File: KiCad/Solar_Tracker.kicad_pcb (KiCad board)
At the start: 2 copper layers, 160 x 100 mm, 116 parts, among them J1 +48V, J10 AZJMP, J11 ELJMP, J12 AZ, J13 CONN_01X03, J2 HOLE, J3 HOLE, J4 EL, J5 HOLE, J6 HOLE, J7 CONN_01X05, J8 GPIO, J9 GPIO, Q1 BUK9M42-60E, Q2 BUK9M42-60E, Q3 BUK9M42-60E, Q4 BUK9M42-60E, Q5 BUK9M42-60E, Q6 BUK9M42-60E, Q7 BUK9M42-60E, Q8 BUK9M42-60E, U1 MER1S4805SC, U10 TLP291, U11 75LBC182, U12 A4927, U2 A4927, U3 Nano, U4 A4927, U5 A4927, U6 MER1S4805SC, U7 TLP291, U8 TLP291, U9 TLP291

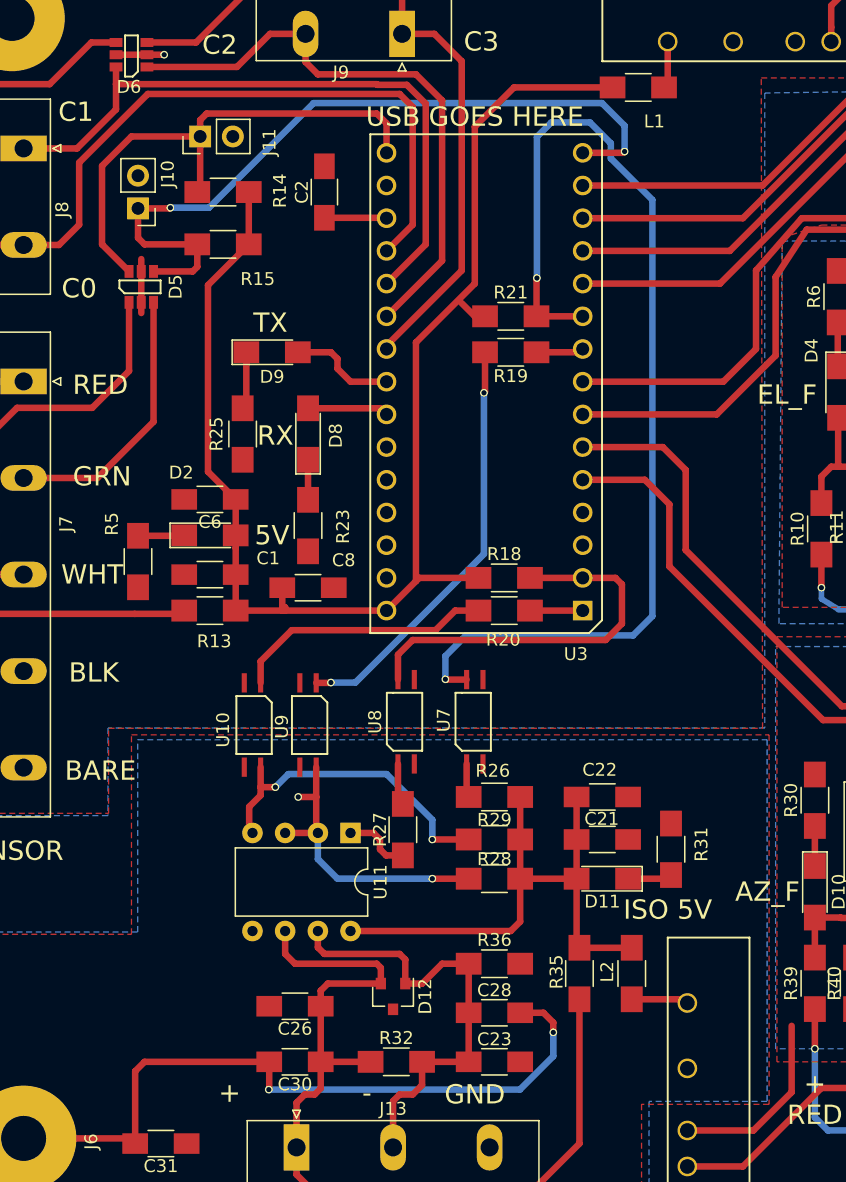
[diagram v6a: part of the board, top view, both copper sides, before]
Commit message: updated RS-485
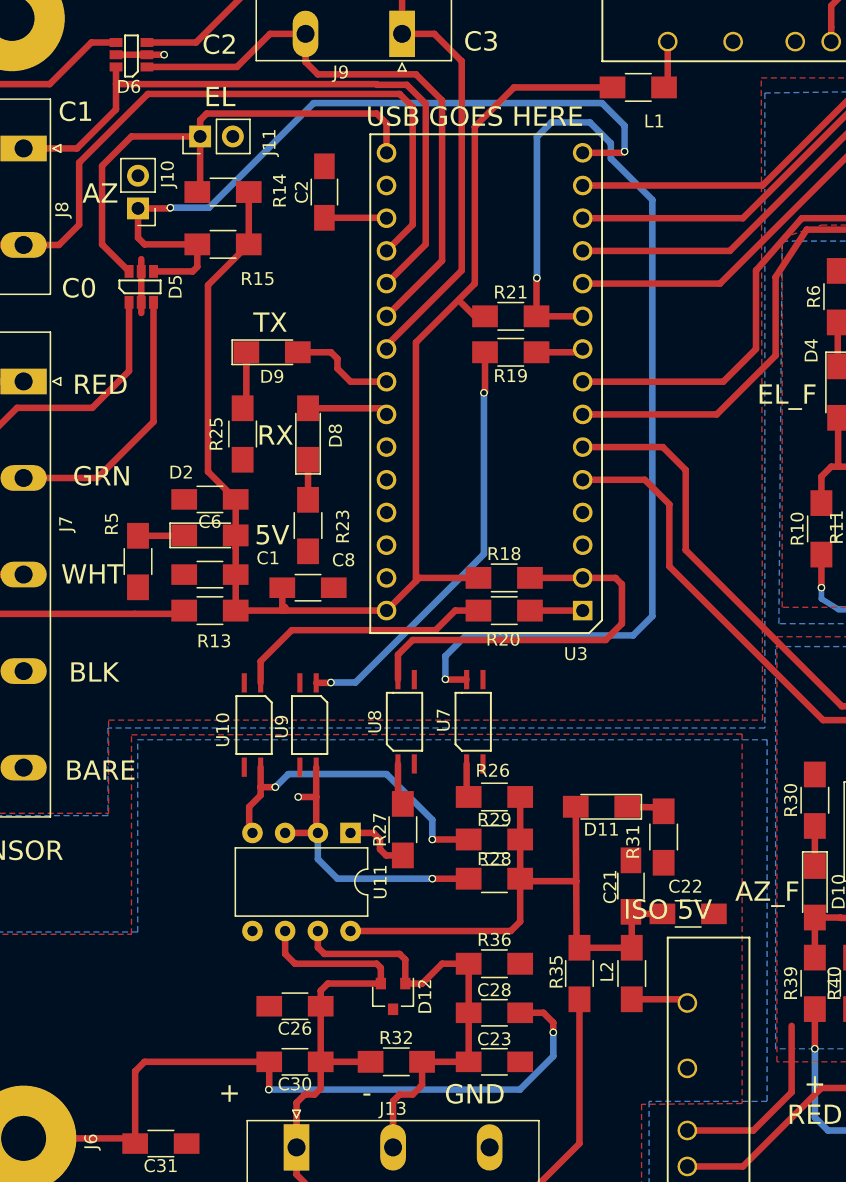
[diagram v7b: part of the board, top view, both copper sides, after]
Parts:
- moved C22 11.3 mm to (70.4, 87.1)
- moved D11 5.59 mm to (63.7, 78.7)
- moved C21 4.25 mm to (66.0, 84.9), turned to 90 degrees
- moved R31 1.11 mm to (68.5, 81.1), turned to 270 degrees
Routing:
- net GND: track 257.3 -> 159.7 mm
- net (no net): track 59.5 -> 157.1 mm
- net +5VD: track 44.2 -> 48.4 mm
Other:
- board text added: "AZ"
- board text added: "CWRU EECS"
- board text added: "EL"
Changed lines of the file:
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@@
   (general
     (links 321)
-    (no_connects 14)
+    (no_connects 15)
     (area 11.924999 11.924999 172.075001 112.075001)
     (thickness 1.6)
-    (drawings 39)
-    (tracks 901)
+    (drawings 42)
+    (tracks 904)
     (zones 0)
     (modules 116)
@@
   )
   (module Capacitors_SMD:C_1206_HandSoldering (layer F.Cu)
-    (at 63.754 81.28)
+    (at 65.9765 84.8995 90)
     (descr "Capacitor SMD 1206, hand soldering")
     (tags "capacitor 1206")
     (attr smd)
-    (fp_text reference C21 (at -0.0508 -1.6002) (layer F.SilkS)
+    (fp_text reference C21 (at -0.0508 -1.6002 90) (layer F.SilkS)
       (effects (font (size 1 1) (thickness 0.15)))
     )
-    (fp_text value 10u (at 0 2) (layer F.Fab)
+    (fp_text value 10u (at 0 2 90) (layer F.Fab)
       (effects (font (size 1 1) (thickness 0.15)))
     )
-    (fp_text user %R (at 0 -1.75) (layer F.Fab)
+    (fp_text user %R (at 0 -1.75 90) (layer F.Fab)
       (effects (font (size 1 1) (thickness 0.15)))
     )
@@
     (fp_line (start 3.25 1.05) (end 3.25 -1.05) (layer F.CrtYd) (width 0.05))
     (fp_line (start 3.25 1.05) (end -3.25 1.05) (layer F.CrtYd) (width 0.05))
-    (pad 1 smd rect (at -2 0) (size 2 1.6) (layers F.Cu F.Paste F.Mask)
+    (pad 1 smd rect (at -2 0 90) (size 2 1.6) (layers F.Cu F.Paste F.Mask)
       (net 14 +5VD))
-    (pad 2 smd rect (at 2 0) (size 2 1.6) (layers F.Cu F.Paste F.Mask)
+    (pad 2 smd rect (at 2 0 90) (size 2 1.6) (layers F.Cu F.Paste F.Mask)
       (net 15 GNDD))
     (model Capacitors_SMD.3dshapes/C_1206.wrl
@@
   )
   (module Capacitors_SMD:C_1206_HandSoldering (layer F.Cu)
-    (at 63.754 77.978)
+    (at 70.4215 87.0585)
     (descr "Capacitor SMD 1206, hand soldering")
     (tags "capacitor 1206")
@@
   )
   (module LEDs:LED_1206_HandSoldering (layer F.Cu)
-    (at 63.754 84.328 180)
+    (at 63.6905 78.74 180)
     (descr "LED SMD 1206, hand soldering")
     (tags "LED 1206")
@@
   )
   (module Resistors_SMD:R_1206_HandSoldering (layer F.Cu)
-    (at 69.088 82.042 90)
+    (at 68.5165 81.0895 270)
     (descr "Resistor SMD 1206, hand soldering")
     (tags "resistor 1206")
     (attr smd)
-    (fp_text reference R31 (at 0.381 2.3622 90) (layer F.SilkS)
+    (fp_text reference R31 (at 0.381 2.3622 270) (layer F.SilkS)
       (effects (font (size 1 1) (thickness 0.15)))
     )
-    (fp_text value 150 (at 0 1.9 90) (layer F.Fab)
+    (fp_text value 150 (at 0 1.9 270) (layer F.Fab)
       (effects (font (size 1 1) (thickness 0.15)))
     )
-    (fp_text user %R (at 0 0 90) (layer F.Fab)
+    (fp_text user %R (at 0 0 270) (layer F.Fab)
       (effects (font (size 0.7 0.7) (thickness 0.105)))
     )
@@
     (fp_line (start 3.25 1.1) (end 3.25 -1.11) (layer F.CrtYd) (width 0.05))
     (fp_line (start 3.25 1.1) (end -3.25 1.1) (layer F.CrtYd) (width 0.05))
-    (pad 1 smd rect (at -2 0 90) (size 2 1.7) (layers F.Cu F.Paste F.Mask)
+    (pad 1 smd rect (at -2 0 270) (size 2 1.7) (layers F.Cu F.Paste F.Mask)
       (net 27 "Net-(D11-Pad1)"))
-    (pad 2 smd rect (at 2 0 90) (size 2 1.7) (layers F.Cu F.Paste F.Mask)
+    (pad 2 smd rect (at 2 0 270) (size 2 1.7) (layers F.Cu F.Paste F.Mask)
       (net 15 GNDD))
     (model ${KISYS3DMOD}/Resistors_SMD.3dshapes/R_1206.wrl
@@
     )
   )
+  (gr_text EL (at 34.036 23.622) (layer F.SilkS)
+    (effects (font (size 1.5 1.5) (thickness 0.3)))
+  )
+  (gr_text AZ (at 24.765 31.115) (layer F.SilkS)
+    (effects (font (size 1.5 1.5) (thickness 0.3)))
+  )
+  (gr_text "CWRU EECS" (at 83.312 60.833) (layer B.SilkS)
+    (effects (font (size 12.7 12.7) (thickness 0.3)) (justify mirror))
+  )
   (gr_text "Documentation Available At:\nhttps://github.com/wnourse05/Lake_Metroparks_Farmpark_Solar_Tracker" (at 159.766 108.077) (layer F.SilkS)
     (effects (font (size 1.5 1.1) (thickness 0.275)) (justify right))
@@
   (segment (start 97.282 61.722) (end 97.282 66.802) (width 3.81) (layer F.Cu) (net 0))
   (segment (start 97.282 66.802) (end 97.663 67.183) (width 3.81) (layer F.Cu) (net 0))
+  (segment (start 169.799 66.929) (end 169.799 29.083) (width 0.508) (layer F.Cu) (net 0))
+  (segment (start 115.697 16.383) (end 115.443 16.129) (width 0.508) (layer F.Cu) (net 0))
+  (segment (start 157.099 16.383) (end 115.697 16.383) (width 0.508) (layer F.Cu) (net 0))
+  (segment (start 169.799 29.083) (end 157.099 16.383) (width 0.508) (layer F.Cu) (net 0))
   (segment (start 37.846 100.711) (end 57.3532 100.711) (width 0.508) (layer B.Cu) (net 1))
   (segment (start 37.878 98.552) (end 37.878 100.679) (width 0.508) (layer F.Cu) (net 1))
@@
   (segment (start 89.916 88.362532) (end 89.916 90.456) (width 0.508) (layer F.Cu) (net 13))
   (segment (start 88.99 87.436532) (end 89.916 88.362532) (width 0.508) (layer F.Cu) (net 13))
+  (segment (start 68.4215 87.0585) (end 66.1355 87.0585) (width 0.508) (layer F.Cu) (net 14) (status C00000))
+  (segment (start 66.1355 87.0585) (end 66.04 87.154) (width 0.508) (layer F.Cu) (net 14) (status C00000))
+  (segment (start 66.04 87.154) (end 66.04 89.694) (width 0.508) (layer F.Cu) (net 14) (status C00000))
+  (segment (start 61.724693 84.518886) (end 57.562886 84.518886) (width 0.508) (layer F.Cu) (net 14))
+  (segment (start 57.562886 84.518886) (end 57.372 84.328) (width 0.508) (layer F.Cu) (net 14))
   (segment (start 44.196 88.392) (end 56.642 88.392) (width 0.508) (layer F.Cu) (net 14))
   (segment (start 57.372 87.662) (end 57.372 84.328) (width 0.508) (layer F.Cu) (net 14))
   (segment (start 56.642 88.392) (end 57.372 87.662) (width 0.508) (layer F.Cu) (net 14))
   (segment (start 61.436 89.154) (end 61.976 89.694) (width 0.508) (layer F.Cu) (net 14))
-  (segment (start 61.754 84.328) (end 61.754 89.472) (width 0.508) (layer F.Cu) (net 14))
+  (segment (start 61.6905 78.74) (end 61.724693 84.518886) (width 0.508) (layer F.Cu) (net 14) (status 10))
+  (segment (start 61.724693 84.518886) (end 61.754 89.472) (width 0.508) (layer F.Cu) (net 14) (status 10))
   (segment (start 61.754 89.472) (end 61.976 89.694) (width 0.508) (layer F.Cu) (net 14))
   (segment (start 66.04 89.694) (end 61.976 89.694) (width 0.508) (layer F.Cu) (net 14))
-  (segment (start 61.754 77.978) (end 61.754 81.28) (width 0.508) (layer F.Cu) (net 14))
-  (segment (start 57.372 84.328) (end 61.754 84.328) (width 0.508) (layer F.Cu) (net 14))
-  (segment (start 61.754 84.328) (end 61.754 81.28) (width 0.508) (layer F.Cu) (net 14))
   (segment (start 57.372 81.28) (end 57.372 84.328) (width 0.508) (layer F.Cu) (net 14))
   (segment (start 57.372 77.978) (end 57.372 81.28) (width 0.508) (layer F.Cu) (net 14))
@@
   (segment (start 32.512 30.766) (end 32.29 30.988) (width 0.508) (layer F.Cu) (net 25))
   (segment (start 80.264 80.232) (end 80.264 83.344) (width 0.508) (layer F.Cu) (net 26))
-  (segment (start 65.754 84.328) (end 68.802 84.328) (width 0.508) (layer F.Cu) (net 27))
-  (segment (start 68.802 84.328) (end 69.088 84.042) (width 0.508) (layer F.Cu) (net 27))
+  (segment (start 65.6905 78.74) (end 68.8025 78.8035) (width 0.508) (layer F.Cu) (net 27) (status 20))
+  (segment (start 68.8025 78.8035) (end 68.5165 79.0895) (width 0.508) (layer F.Cu) (net 27) (status 30))
   (segment (start 68.834 19.304) (end 68.834 22.574) (width 0.508) (layer F.Cu) (net 28))
   (segment (start 68.834 22.574) (end 68.548 22.86) (width 0.508) (layer F.Cu) (net 28))
@@
   (segment (start 77.216 43.688) (end 77.216 37.592) (width 0.508) (layer F.Cu) (net 127))
   (segment (start 72.644 48.26) (end 77.216 43.688) (width 0.508) (layer F.Cu) (net 127))
-  (segment (start 169.799 66.929) (end 169.799 29.083) (width 0.508) (layer F.Cu) (net 132))
-  (segment (start 115.697 16.383) (end 115.443 16.129) (width 0.508) (layer F.Cu) (net 132))
-  (segment (start 157.099 16.383) (end 115.697 16.383) (width 0.508) (layer F.Cu) (net 132))
-  (segment (start 169.799 29.083) (end 157.099 16.383) (width 0.508) (layer F.Cu) (net 132))
   (segment (start 28.378 20.32) (end 29.718 20.32) (width 0.508) (layer F.Cu) (net 132))
   (via (at 29.718 20.32) (size 0.6) (drill 0.4) (layers F.Cu B.Cu) (net 132))
@@
     (polygon
       (pts
-        (xy 76.708 101.854) (xy 66.802 101.854) (xy 66.802 112.014) (xy 11.938 112.014) (xy 11.938 88.646)
-        (xy 27.178 88.646) (xy 27.178 73.152) (xy 76.708 73.152)
+        (xy 74.6125 101.7905) (xy 66.802 101.854) (xy 66.802 112.014) (xy 11.938 112.014) (xy 11.938 88.646)
+        (xy 27.178 88.646) (xy 27.178 73.152) (xy 74.6125 73.0885)
       )
     )
@@
     (polygon
       (pts
-        (xy 13.208 13.208) (xy 13.208 79.248) (xy 25.4 79.248) (xy 25.4 72.644) (xy 76.2 72.644)
+        (xy 13.208 13.208) (xy 13.208 79.248) (xy 25.4 79.248) (xy 25.4 72.009) (xy 76.2 72.009)
         (xy 76.0984 22.1234) (xy 116.7384 22.1234) (xy 116.84 12.7) (xy 13.208 12.7) (xy 13.208 15.748)
       )

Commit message: gerbers
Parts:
- moved R5 49.7 mm to (56.1, 19.0)
- moved C8 47.6 mm to (61.7, 18.9), turned to 90 degrees
- moved D2 46.5 mm to (58.9, 18.9), turned to 270 degrees
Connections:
- D5 pad 1: A0 -> A7
- D5 pad 3: A1 -> A6
- J7 pad 2: A1 -> A6
- J7 pad 3: A0 -> A7
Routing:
- net A7: track 0.00 -> 63.6 mm
- net A6: track 0.00 -> 50.0 mm
- net A0: track 32.4 -> 0.00 mm
- net (no net): track 157.1 -> 183.3 mm
- net A1: track 21.2 -> 0.00 mm
- net +5V: track 108.4 -> 104.3 mm
- net GND: track 159.7 -> 160.9 mm
- net Net-(D2-Pad1): track 3.60 -> 2.82 mm
